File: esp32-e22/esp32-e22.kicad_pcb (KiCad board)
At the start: 2 copper layers, 6 parts

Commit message: update
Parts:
- removed REF** (x3): PinHeader_1x04_P2.54mm_Vertical, Connector_PinHeader_2.54mm:PinHeader_1x04_P2.54mm_Vertical
- removed REF**: PinHeader_1x03_P2.54mm_Vertical, Connector_PinHeader_2.54mm:PinHeader_1x03_P2.54mm_Vertical
- removed REF**: ESP32-DevKitC, E22:ESP32-DevKitC
- removed REF**: E22-400M33S, E22:E22-400M33S
- added J1: Conn_01x04_Socket, Connector_PinHeader_2.54mm:PinHeader_1x04_P2.54mm_Vertical, F.Cu at (153.9, 121.8)
- added J2: Conn_01x04_Socket, Connector_PinHeader_2.54mm:PinHeader_1x04_P2.54mm_Vertical, F.Cu at (162.7, 121.9)
- added J3: Conn_01x04_Socket, Connector_PinHeader_2.54mm:PinHeader_1x04_P2.54mm_Vertical, F.Cu at (167.3, 121.9)
- added J4: Conn_01x03_Socket, Connector_PinHeader_2.54mm:PinHeader_1x03_P2.54mm_Vertical, F.Cu at (172.0, 121.9)
- added J5: SMA, Connector_Coaxial:SMA_Amphenol_901-143_Horizontal, F.Cu at (125.0, 48.5)
- added J6: Conn_01x01_Socket, Connector_PinHeader_2.54mm:PinHeader_1x01_P2.54mm_Vertical, F.Cu at (146.0, 83.0)
- added U1: E22-40033S, E22:E22-400M33S, F.Cu at (133.1, 69.0)
- added U2: ESP32-DevKitC, E22:ESP32-DevKitC, F.Cu at (124.0, 96.0)
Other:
- board outline added: 44 x 100 mm

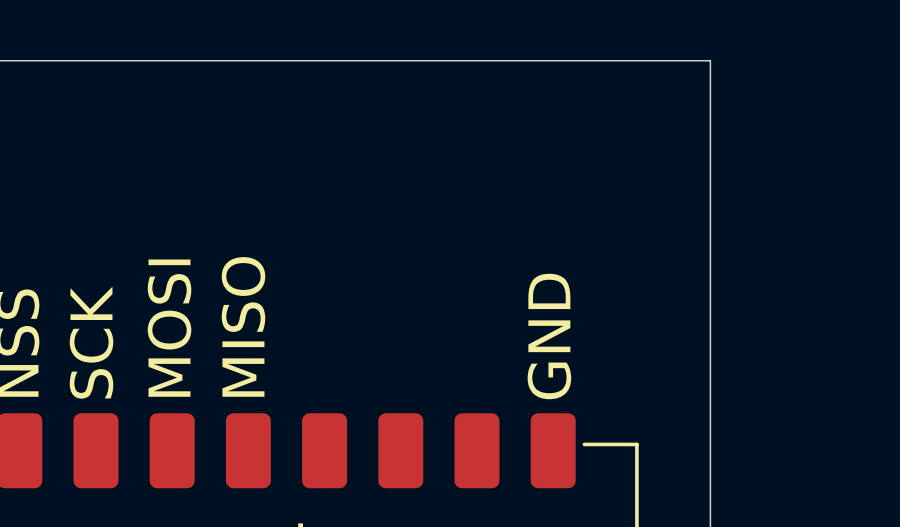
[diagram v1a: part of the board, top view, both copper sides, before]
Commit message: add usb-c connector
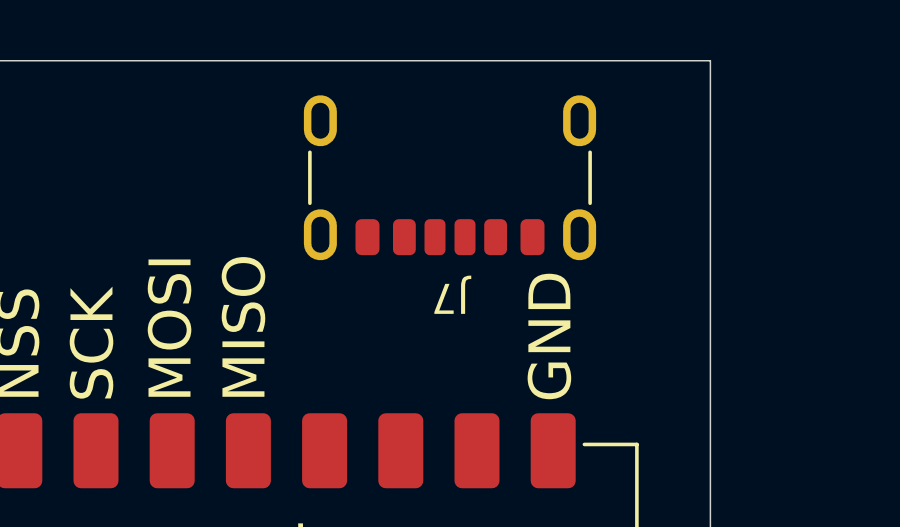
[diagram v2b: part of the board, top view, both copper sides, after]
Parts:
- added J7: USB_C_Receptacle_PowerOnly_6P, Connector_USB:USB_C_Receptacle_GCT_USB4125-xx-x-0190_6P_TopMnt_Horizontal, F.Cu at (149.3, 46.8)

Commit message: update to OE3WAS V2.0.2
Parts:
- added C1: 470µF, Capacitor_THT:CP_Radial_D8.0mm_P5.00mm, F.Cu at (185.0, 62.2)
- added C1: 470µF, Capacitor_THT:CP_Radial_D8.0mm_P5.00mm, F.Cu at (165.2, 63.5)
- added C2: 100nF, Capacitor_THT:C_Disc_D4.7mm_W2.5mm_P5.00mm, F.Cu at (184.1, 74.6)
- added C2: 100nF, Capacitor_THT:C_Disc_D4.7mm_W2.5mm_P5.00mm, F.Cu at (175.3, 84.8)
- added C3: 100nF, Capacitor_THT:C_Disc_D4.7mm_W2.5mm_P5.00mm, F.Cu at (175.3, 88.9)
- added C3: 100nF, Capacitor_THT:C_Disc_D4.7mm_W2.5mm_P5.00mm, F.Cu at (184.1, 78.7)
- added J6: Conn_01x02_Pin, Connector_PinHeader_2.54mm:PinHeader_1x02_P2.54mm_Vertical, F.Cu at (193.0, 74.9)
- added J8: Conn_01x04_Socket, Connector_PinHeader_2.54mm:PinHeader_1x04_P2.54mm_Vertical, F.Cu at (180.3, 110.5)
- added JP3: Jumper_2_Small_Open, TestPoint:TestPoint_2Pads_Pitch2.54mm_Drill0.8mm, F.Cu at (165.1, 98.2)
- added JP4: Jumper_2_Small_Open, TestPoint:TestPoint_2Pads_Pitch2.54mm_Drill0.8mm, F.Cu at (165.1, 101.6)
- added R1: 5.1k, Resistor_THT:R_Axial_DIN0207_L6.3mm_D2.5mm_P7.62mm_Horizontal, F.Cu at (164.8, 76.8)
- added R2: 5.1k, Resistor_THT:R_Axial_DIN0207_L6.3mm_D2.5mm_P7.62mm_Horizontal, F.Cu at (164.8, 80.8)
- added SW1: SW_Push, Button_Switch_THT:SW_PUSH_6mm, F.Cu at (165.2, 84.8)
- moved J6 34.6 mm to (177.8, 96.5)
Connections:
- net E22_BUSY renamed /E22_BUSY
- net E22_DIO1 renamed /E22_DIO1
- net E22_NRST renamed /E22_NRST
- net E22_NSS renamed /E22_NSS
- net E22_RXEN renamed /E22_RXEN
- net E22_SCK renamed /E22_SCK
- net E22_TXEN renamed /E22_TXEN
- net GPS_RX renamed /GPS_RX
- net GPS_TX renamed /GPS_TX
- net MISO renamed /MISO
- net MOSI renamed /MOSI
- net ONEWIRE renamed /OneWire
- J2 pad 3: SCL -> Net-(J2-Pin_3)
- J2 pad 4: SDA -> Net-(J2-Pin_4)
- J3 pad 3: SCL -> /SCL
- J3 pad 4: SDA -> /SDA
- J5 pad 2: unconnected-(J5-Ext-Pad2) -> GND
- J7 pad S1: unconnected-(J7-SHIELD-PadS1) -> GND
- U2 pad 33: SDA -> /SDA
- U2 pad 36: SCL -> /SCL

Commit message: update to OE3WAS V2.0.3
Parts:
- removed the C1 at (165.2, 63.5)
- removed the C2 at (175.3, 84.8)
- removed the C3 at (175.3, 88.9)
- removed JP3, JP4: Jumper_2_Small_Open, TestPoint:TestPoint_2Pads_Pitch2.54mm_Drill0.8mm
- added C4: 100nF, Capacitor_THT:C_Disc_D4.7mm_W2.5mm_P5.00mm, F.Cu at (184.2, 82.5)
- added JP1: Jumper_2_Small_Bridged, TestPoint:TestPoint_2Pads_Pitch2.54mm_Drill0.8mm, F.Cu at (189.2, 91.9)
- added JP2: Jumper_2_Small_Bridged, TestPoint:TestPoint_2Pads_Pitch2.54mm_Drill0.8mm, F.Cu at (189.2, 95.2)
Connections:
- J2 pad 1: +3.3V -> Net-(J2-Pin_1)
- J2 pad 2: GND -> Net-(J2-Pin_2)
- J2 pad 3: Net-(J2-Pin_3) -> /SCL
- J2 pad 4: Net-(J2-Pin_4) -> /SDA

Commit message: fixed some missing footprints -> V2.0.5
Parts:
- removed the J6 at (177.8, 96.5)
- removed the J6 at (193.0, 74.9)
- added J6: Conn_01x02_Socket, Connector_PinHeader_2.54mm:PinHeader_1x02_P2.54mm_Vertical, F.Cu at (169.0, 100.5)
- added J9: Conn_01x02_Socket, Connector_PinHeader_2.54mm:PinHeader_1x02_P2.54mm_Vertical, F.Cu at (201.0, 83.5)

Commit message: update to v2.0.6
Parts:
- added C5: 100nF, Capacitor_THT:C_Disc_D4.7mm_W2.5mm_P5.00mm, F.Cu at (114.3, 114.4)
- added C6: 10µF, Capacitor_THT:CP_Radial_D6.3mm_P2.50mm, F.Cu at (121.9, 86.4)
- added J10: Conn_01x02_Socket, Connector_PinHeader_2.54mm:PinHeader_1x02_P2.54mm_Vertical, F.Cu at (108.0, 115.6)
- added R3: 5.1k, Resistor_THT:R_Axial_DIN0207_L6.3mm_D2.5mm_P7.62mm_Horizontal, F.Cu at (106.7, 111.8)
- added R4: 5.1k, Resistor_THT:R_Axial_DIN0207_L6.3mm_D2.5mm_P7.62mm_Horizontal, F.Cu at (118.1, 111.8)
- J9: footprint Connector_PinHeader_2.54mm:PinHeader_1x02_P2.54mm_Vertical -> TerminalBlock_Phoenix:TerminalBlock_Phoenix_MKDS-1,5-2-5.08_1x02_P5.08mm_Horizontal
- moved J7 94.5 mm to (161.3, 140.6), turned to 0 degrees
- moved C3 68.2 mm to (153.7, 139.7), turned to -90 degrees
- moved J4 65.4 mm to (111.8, 96.5)
- moved SW1 64.8 mm to (112.3, 122.2)
- moved J9 62.4 mm to (174.0, 139.7)
- moved R1 58.0 mm to (161.3, 134.6)
- moved R2 50.1 mm to (161.3, 130.8)
- moved J3 44.5 mm to (166.4, 77.5), turned to 90 degrees
- moved J8 43.0 mm to (166.4, 69.8), turned to 90 degrees
- moved C1 42.7 mm to (149.9, 86.4)
- moved J1 38.8 mm to (116.8, 133.4)
- moved C2 38.7 mm to (149.9, 92.7)
- moved J6 34.8 mm to (137.2, 86.4), turned to -90 degrees
- moved JP2 23.2 mm to (166.4, 99.1), turned to -90 degrees
- moved JP1 22.5 mm to (168.9, 101.6), turned to 90 degrees
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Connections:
- C1 pad 1: GND -> +5V
- C1 pad 2: +5V -> GND
- C4 pad 1: +5V -> +3.3V
- U2 pad 2: unconnected-(U2-CHIP_PU-Pad2) -> Net-(U2-CHIP_PU)
- U2 pad 7: unconnected-(U2-32K_XP/GPIO32/ADC1_CH4-Pad7) -> Net-(U2-32K_XP/GPIO32/ADC1_CH4)
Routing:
- net GND: track 0.00 -> 398.8 mm
- net +3.3V: track 0.00 -> 135.8 mm
- net +5V: track 0.00 -> 123.4 mm
- net /E22_BUSY: track 0.00 -> 76.3 mm, vias 0 -> 1
- net /E22_NRST: track 0.00 -> 76.0 mm, vias 0 -> 1
- net /E22_DIO1: track 0.00 -> 73.9 mm, vias 0 -> 1
- net /E22_NSS: track 0.00 -> 70.6 mm, vias 0 -> 1
- net /E22_SCK: track 0.00 -> 67.0 mm, vias 0 -> 1
- net /MISO: track 0.00 -> 62.3 mm, vias 0 -> 1
- net /SDA: track 0.00 -> 62.1 mm
- net /SCL: track 0.00 -> 61.6 mm
- net /E22_TXEN: track 0.00 -> 61.1 mm, vias 0 -> 1
- net /E22_RXEN: track 0.00 -> 53.5 mm, vias 0 -> 1
- net /MOSI: track 0.00 -> 48.2 mm, vias 0 -> 1
- net /GPS_TX: track 0.00 -> 39.9 mm
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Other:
- board size 44 x 100 mm -> 83.8 x 104.1 mm

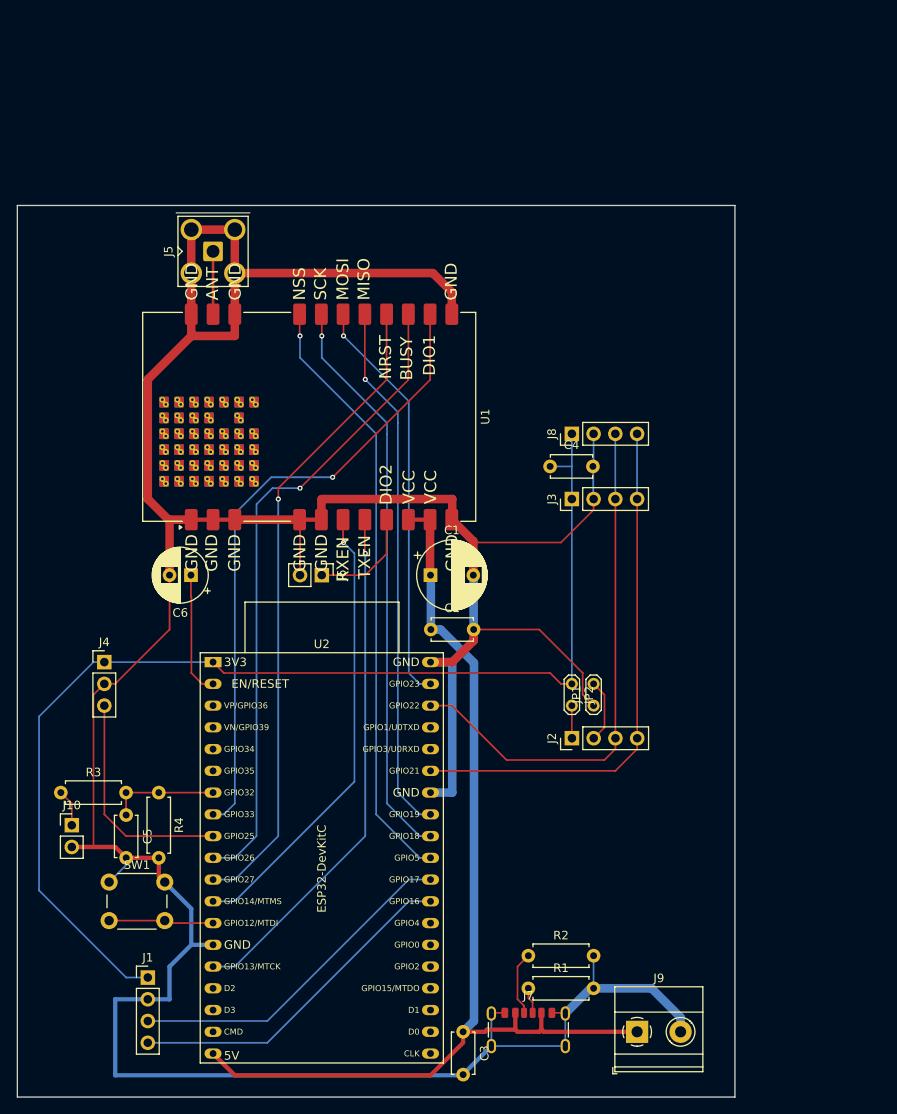
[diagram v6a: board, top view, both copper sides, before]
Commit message: update to v2.0.7
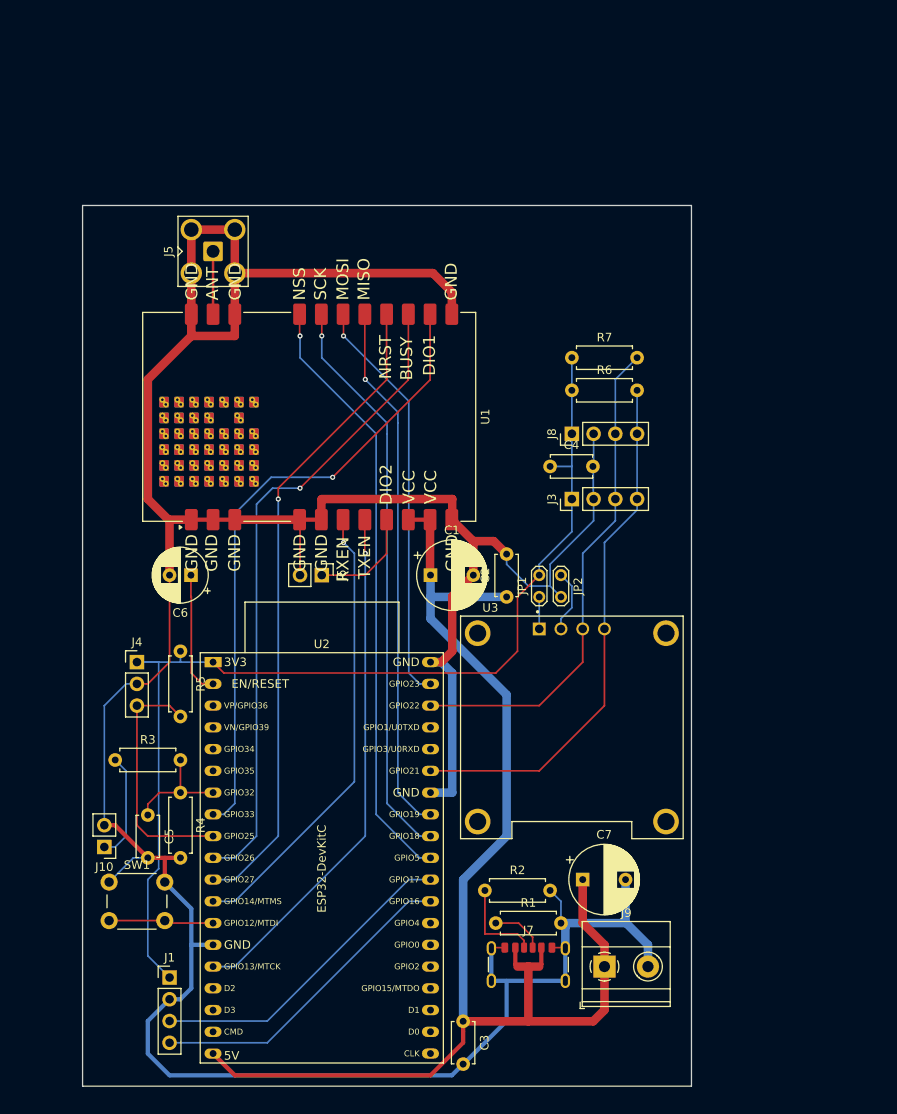
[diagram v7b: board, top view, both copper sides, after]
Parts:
- removed J2: Conn_01x04_Socket, Connector_PinHeader_2.54mm:PinHeader_1x04_P2.54mm_Vertical
- added C7: 470µF, Capacitor_THT:CP_Radial_D8.0mm_P5.00mm, F.Cu at (167.6, 121.9)
- added R5: 4k7, Resistor_THT:R_Axial_DIN0207_L6.3mm_D2.5mm_P7.62mm_Horizontal, F.Cu at (120.7, 95.2)
- added R6: 10k, Resistor_THT:R_Axial_DIN0207_L6.3mm_D2.5mm_P7.62mm_Horizontal, F.Cu at (166.4, 64.8)
- added R7: 10k, Resistor_THT:R_Axial_DIN0207_L6.3mm_D2.5mm_P7.62mm_Horizontal, F.Cu at (166.4, 61.0)
- added U3: DM-OLED096-636, E22:DM-OLED096-636, F.Cu at (166.4, 104.1)
- R1, R2, R3, R4: value 5.1k -> 5k1
- moved JP1 14.2 mm to (162.6, 88.9)
- moved JP2 12.8 mm to (165.1, 86.4)
- moved C2 9.64 mm to (158.8, 88.9), turned to 90 degrees
- moved R2 9.16 mm to (156.2, 123.2)
- moved R1 8.52 mm to (157.5, 127.0)
- moved J9 8.52 mm to (170.2, 132.1)
- moved J7 7.62 mm to (161.3, 132.9)
- moved R3 7.41 mm to (113.0, 108.0)
- moved J10 4.57 mm to (111.8, 118.1), turned to 180 degrees
- moved J4 3.81 mm to (115.6, 96.5)
- moved J1 2.54 mm to (119.4, 133.4)
- moved C5 2.53 mm to (116.8, 114.4)
- moved R4 2.53 mm to (120.7, 111.8)
- moved C3 1.23 mm to (153.7, 138.5)
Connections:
- JP1 pad 1: GND -> Net-(JP1-A)
- JP1 pad 2: Net-(J2-Pin_2) -> +3.3V
- JP2 pad 1: +3.3V -> Net-(JP2-A)
- JP2 pad 2: Net-(J2-Pin_1) -> GND
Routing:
- net +5V: track 123.4 -> 157.1 mm
- net GND: track 398.8 -> 388.8 mm
- net Net-(J10-Pin_1): track 4.35 -> 12.5 mm
- net Net-(J2-Pin_2): track 7.40 -> 0.00 mm
- net Net-(JP2-A): track 0.00 -> 7.33 mm
- net +3.3V: track 135.8 -> 128.6 mm
- net Net-(J2-Pin_1): track 3.83 -> 0.00 mm
- net Net-(JP1-A): track 0.00 -> 3.74 mm
- net /SCL: track 61.6 -> 58.1 mm
- net Net-(J7-CC1): track 7.52 -> 10.8 mm
- net Net-(J7-CC2): track 3.07 -> 6.22 mm
- net /OneWire: track 26.5 -> 29.0 mm
- net /GPS_TX: track 39.9 -> 37.3 mm
- net /GPS_RX: track 39.9 -> 37.3 mm
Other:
- board size 83.8 x 104.1 mm -> 71.1 x 102.9 mm

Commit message: update to v2.0.8
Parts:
- added D1: D_Schottky_Small, Diode_THT:D_A-405_P7.62mm_Horizontal, F.Cu at (188.0, 79.4)
- added D2: SD05_SOD323, Diode_SMD:D_SOD-523, F.Cu at (188.6, 84.5)
- moved R2 4.02 mm to (157.5, 127.0)
- moved R1 3.81 mm to (157.5, 123.2)
- moved J1 2.55 mm to (119.4, 130.8)
- moved C7 1.27 mm to (168.9, 121.9)
- moved R5 1.27 mm to (120.7, 94.0)
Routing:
- net GND: track 388.8 -> 419.5 mm
- net +5V: track 157.1 -> 149.3 mm
- net Net-(J7-CC1): track 10.8 -> 4.98 mm
- net Net-(U2-CHIP_PU): track 14.6 -> 18.9 mm
- net /OneWire: track 29.0 -> 25.5 mm
- net Net-(J7-CC2): track 6.22 -> 8.46 mm
- net /GPS_TX: track 37.3 -> 36.3 mm
- net /GPS_RX: track 37.3 -> 36.3 mm
- net /E22_BUSY: track 76.3 -> 75.6 mm
- net /MISO: track 62.3 -> 63.1 mm
- net Net-(U2-32K_XP/GPIO32/ADC1_CH4): track 13.3 -> 12.5 mm
- net /MOSI: track 48.2 -> 48.9 mm
- net /E22_SCK: track 67.0 -> 67.7 mm
- net /E22_NSS: track 70.6 -> 71.3 mm
